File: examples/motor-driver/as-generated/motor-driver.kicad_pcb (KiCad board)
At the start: 2 copper layers, 88 x 50 mm, 12 parts, among them J1 VM 2.7-10.8V, J2 MOTOR A, J3 MOTOR B, J4 LOGIC, U1 DRV8833PW

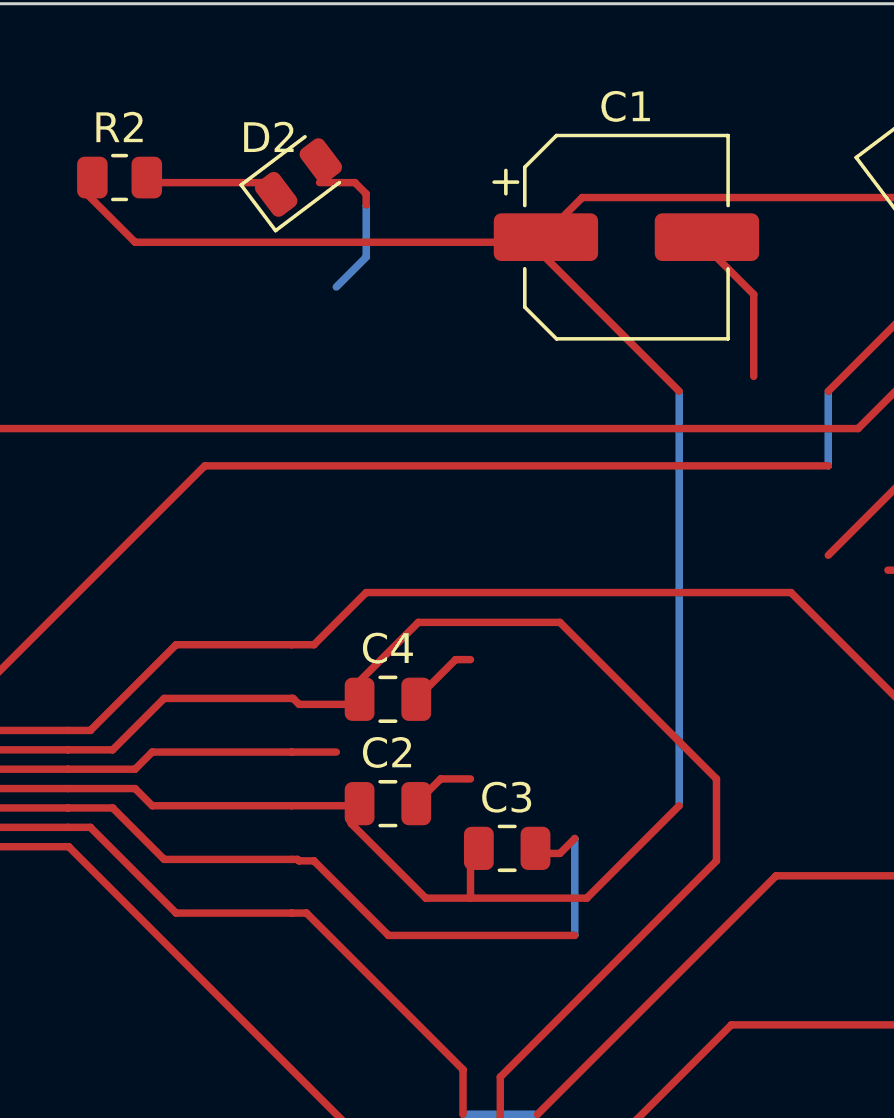
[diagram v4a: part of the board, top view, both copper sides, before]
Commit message: Give the vias room to stand beside the lands
Following the via-in-pad ban, the FPGA board stopped routing: five
attempts, five different nets, each one out of lanes in the corridor
between the FPGA's east escape fan and the codec's west one. Three
changes, in the order a layout would make them.

The via spacing was guesswork and is now the fab's. Hole to hole goes
from 1.2 mm to 0.9, which at the shipped 0.8/0.4 via leaves half a
millimetre of laminate between barrels - the ordinary minimum - and in a
1 mm-pitch escape comb is the difference between a lane and no lane.
What a via keeps off a land it may not sit in is its own radius plus a
solder-mask dam rather than the track clearance: the copper either side
may well be the same net, and what has to be true is that the mask can
part the barrel from the land.

Every decoupling capacitor now has its ground via placed against its own
pad rather than nine of them asking the search for one, and where the
via goes is chosen rather than fixed: `anchor_site` takes the nearest
position that clears everything already placed, fanning either side of
the direction facing off the part. A fixed offset walled off the
corridor its neighbour's supply needed - the via was legal, and it was
in the way.

And the seven parts sitting inside that corridor - four decoupling
capacitors, the two 1.2 V ones and the LED resistor - move four
millimetres south into the empty band below it. Twelve lanes leaving the
FPGA and ten arriving at the codec have eleven millimetres to cross in;
what a hand would do first is stop parking capacitors in the middle of
that, and it is the floorplan half of the debt this board's own README
has been carrying.

Co-Authored-By: Claude Fable 5 <noreply@anthropic.com>
Claude-Session: https://claude.ai/code/session_01DUj7Ltu92tWg159mCSacwY
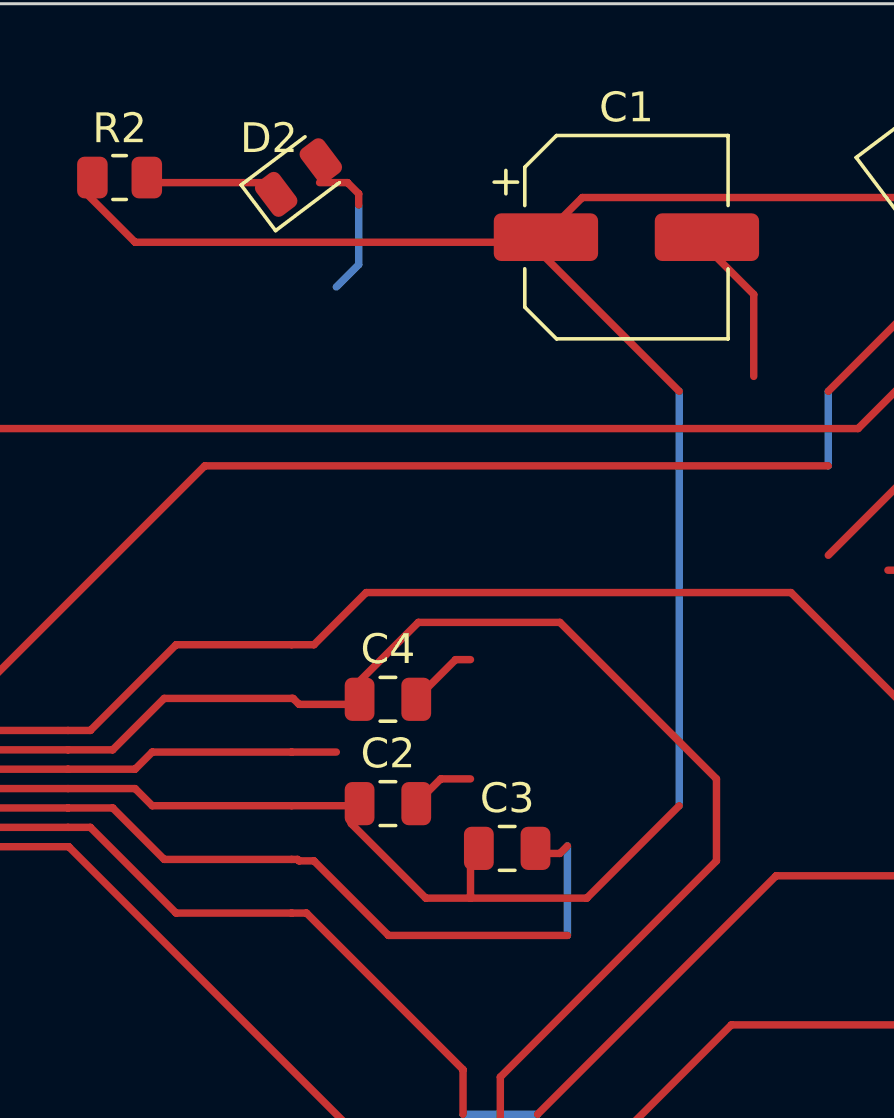
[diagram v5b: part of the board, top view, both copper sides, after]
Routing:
- net /VCP: track 27.4 -> 26.6 mm
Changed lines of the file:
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@@
 	(segment (start 181.75 97.0) (end 178.75 100.0) (width 0.25) (layer "F.Cu") (net 1))
 	(segment (start 178.75 100.0) (end 178.0 100.0) (width 0.25) (layer "F.Cu") (net 1))
-	(segment (start 158.9375 66.0) (end 160.125 66.0) (width 0.25) (layer "F.Cu") (net 1))
-	(segment (start 160.125 66.0) (end 160.5 66.375) (width 0.25) (layer "F.Cu") (net 1))
-	(segment (start 160.5 66.375) (end 160.5 66.75) (width 0.25) (layer "F.Cu") (net 1))
-	(segment (start 160.5 66.75) (end 160.5 68.5) (width 0.25) (layer "B.Cu") (net 1))
-	(segment (start 160.5 68.5) (end 159.5 69.5) (width 0.25) (layer "B.Cu") (net 1))
+	(segment (start 158.9375 66.0) (end 159.875 66.0) (width 0.25) (layer "F.Cu") (net 1))
+	(segment (start 159.875 66.0) (end 160.25 66.375) (width 0.25) (layer "F.Cu") (net 1))
+	(segment (start 160.25 66.375) (end 160.25 66.75) (width 0.25) (layer "F.Cu") (net 1))
+	(segment (start 160.25 66.75) (end 160.25 68.75) (width 0.25) (layer "B.Cu") (net 1))
+	(segment (start 160.25 68.75) (end 159.5 69.5) (width 0.25) (layer "B.Cu") (net 1))
 	(segment (start 141.1375 83.725) (end 137.5 83.725) (width 0.25) (layer "F.Cu") (net 15))
 	(segment (start 137.5 83.725) (end 134.875 81.1) (width 0.25) (layer "F.Cu") (net 15))
@@
 	(segment (start 158.25 88.75) (end 158.75 88.75) (width 0.25) (layer "F.Cu") (net 11))
 	(segment (start 158.75 88.75) (end 161.25 91.25) (width 0.25) (layer "F.Cu") (net 11))
-	(segment (start 161.25 91.25) (end 167.5 91.25) (width 0.25) (layer "F.Cu") (net 11))
+	(segment (start 161.25 91.25) (end 167.25 91.25) (width 0.25) (layer "F.Cu") (net 11))
 	(segment (start 146.8625 87.625) (end 147.0925 87.625) (width 0.25) (layer "F.Cu") (net 7))
 	(segment (start 147.0925 87.625) (end 150.5 87.625) (width 0.25) (layer "F.Cu") (net 7))
@@
 	(segment (start 151.0 66.25) (end 152.75 68.0) (width 0.25) (layer "F.Cu") (net 13))
 	(segment (start 152.75 68.0) (end 166.3 68.0) (width 0.25) (layer "F.Cu") (net 13))
-	(segment (start 167.5 91.25) (end 167.5 88.0) (width 0.25) (layer "B.Cu") (net 11))
-	(segment (start 167.5 88.0) (end 167.0 88.5) (width 0.25) (layer "F.Cu") (net 11))
+	(segment (start 167.25 91.25) (end 167.25 88.25) (width 0.25) (layer "B.Cu") (net 11))
+	(segment (start 167.25 88.25) (end 167.0 88.5) (width 0.25) (layer "F.Cu") (net 11))
 	(segment (start 167.0 88.5) (end 166.18 88.5) (width 0.25) (layer "F.Cu") (net 11))
 	(segment (start 166.18 88.5) (end 165.95 88.5) (width 0.25) (layer "F.Cu") (net 11))

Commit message: Let KiCad fill the plane, and check the fill we actually ship
The reviewer saw copper pushing in between an 0603's pads and asked
whether DRC had been run at all. It had, and it was green, and both
things were true because the check and the drawing were looking at
different polygons.

The fill in the file was ours: a sweep of the pour outline with
everything of another net subtracted, written because a note here said
KiCad's own filler needs a display the container has not got. It does
not - `pcbnew`'s `ZONE_FILLER` runs headless in both images, and always
did by the time that note was written. Meanwhile `pcb drc` was passing
`--refill-zones`, so KiCad threw our polygons away and reported on a
fill of its own. Nobody was checking the one that ships, and it had
drifted: copper 0.075 mm from a foreign pad where the rule says 0.25,
and - measured just now with the refill turned off - two hundred pieces
of copper KiCad calls isolated.

So the zone is declared and left empty, and KiCad fills it: clearance,
minimum width and thermal relief all come from the board's own rules
instead of this file's idea of them. And `drc()` no longer refills a
board whose zones are already filled, because that fill is what goes to
the fab and what the plots draw. A board with an unfilled zone is still
refilled - otherwise every pad on that net reads as unconnected and the
report is noise - and `layout.unfilled_zone` says the file is
incomplete.

All five boards regenerate clean on both matrix versions against their
own committed fill: no errors, nothing unconnected, no isolated copper.
The plane no longer reaches between the passives' lands, and every
through-hole ground pad now has the four spokes of a thermal relief, so
an iron can bring the joint up without heating the whole plane.

The parser gains a pad's corner radius while measuring this, because a
roundrect land's bounding box is a quarter of a millimetre away from
where its copper is.

Co-Authored-By: Claude Fable 5 <noreply@anthr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
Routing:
- net GND: track 68.0 -> 66.2 mm
- net /LED_A: track 4.15 -> 5.99 mm

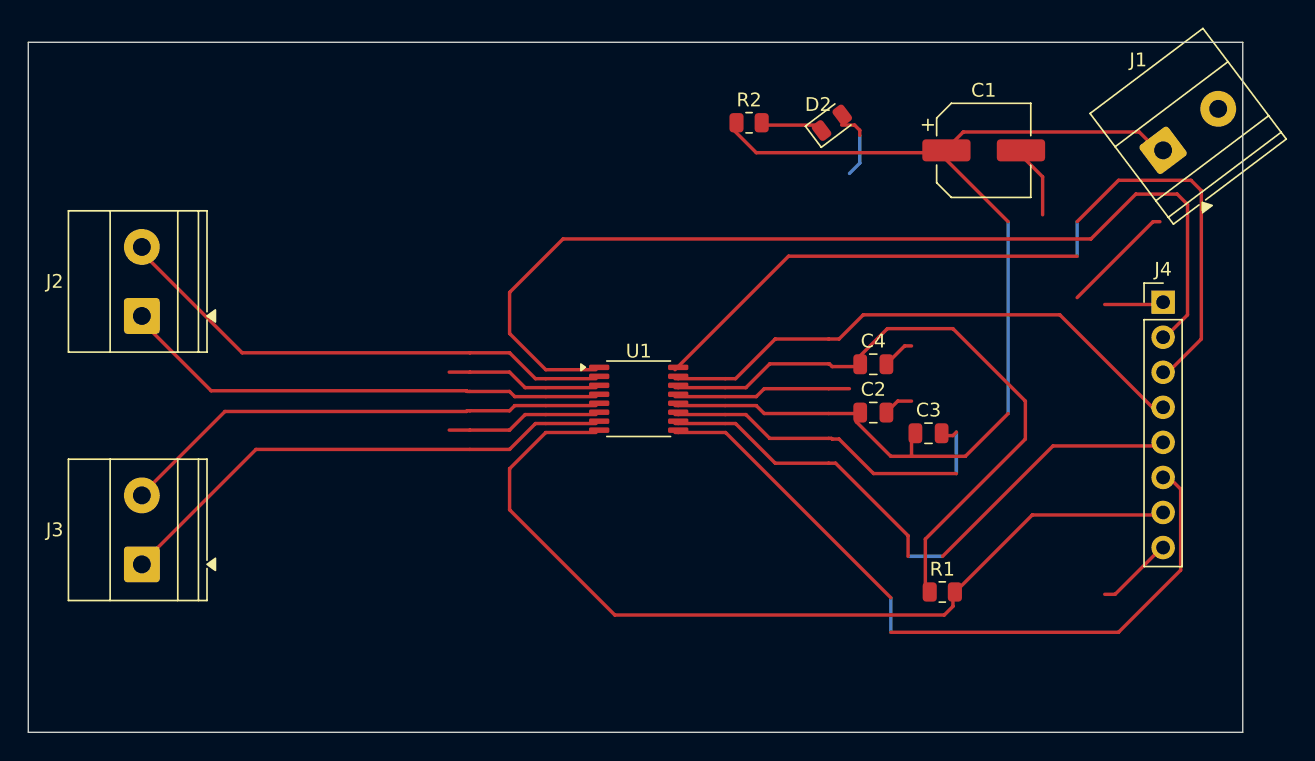
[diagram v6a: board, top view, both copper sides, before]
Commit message: Relieve the pads, fillet the joints, and give the board its screw holes
Three of the reviewer's manufacturing points, and they largely fall out
of the one before it - once KiCad fills the plane, the thermal relief it
was already asked for in the file actually appears.

**Thermal relief.** The zones said thermal all along; our own filler
ignored it and flooded every land solid. KiCad's does not, so every
through-hole ground pad now sits in a gap bridged by four spokes and an
iron can bring the joint up without heating a hundred square millimetres
of copper. `layout.solid_pad_connection` reports the setting when a
board turns it off: drilled pads only, because a surface pad reflows in
an oven that is heating the plane anyway and flooding it is often the
better thermal answer.

**Teardrops.** A track entering a land is a step change in width, and a
step change is where copper tears - the connector gets levered on and
off, the drill wanders, and the crack starts at the corner. `_teardrops`
replaces the first stretch of each run with a three-step taper into the
land, checked against its neighbours before it is kept, so a fillet
never eats the clearance a fine-pitch escape needs. It *replaces* rather
than overlays: laying the taper on top of the run drew the same copper
twice, and `route.acute_angle` reported all thirty of them, correctly.
`route.mixed_track_widths` learns what a fillet looks like so a properly
filleted board does not read as one nobody decided the width of.

**Mounting holes.** Four M3 holes near the corners, placed before the
router runs because they are obstacles, and slid along the edges or a
little inboard where a connector body has the corner - the motor board
and the op-amp take three, which is what those floorplans have room for.
Grounded on the motor driver, whose chassis is metal and part of the
shield, plain on the rest: bonding the enclosure to the reference is the
enclosure's decision, not the board's.

Two things that fell out of placing par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
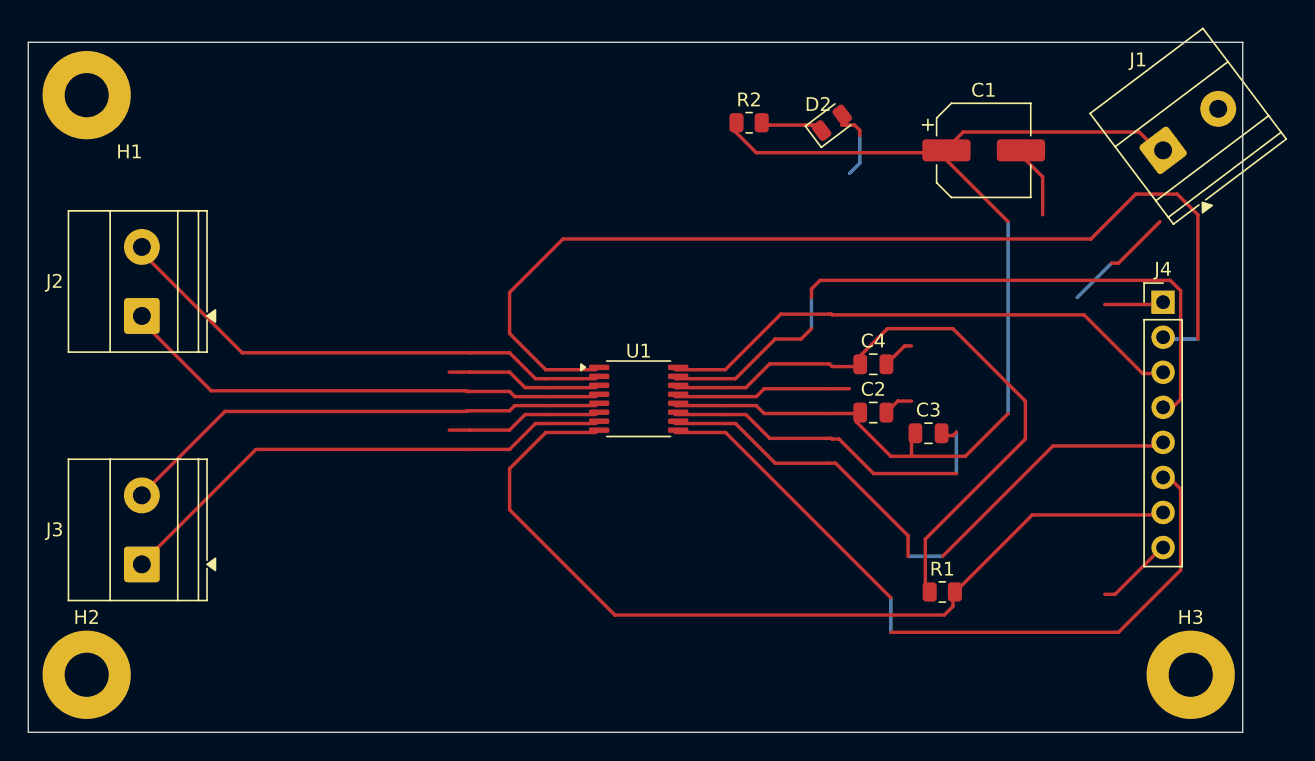
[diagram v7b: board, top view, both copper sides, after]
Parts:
- added H1: M33, MountingHole:MountingHole_3.2mm_M3_Pad, F.Cu at (104.2, 63.8)
- added H2: M33, MountingHole:MountingHole_3.2mm_M3_Pad, F.Cu at (104.2, 105.8)
- added H3: M33, MountingHole:MountingHole_3.2mm_M3_Pad, F.Cu at (184.2, 105.8)
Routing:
- net /AIN1: track 60.4 -> 38.6 mm
- net /AIN2: track 39.9 -> 51.3 mm
- net /nSLEEP: track 73.5 -> 75.5 mm

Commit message: Give the assembly machine something to aim at
Fiducials: three copper dots in bare mask windows, near three different
corners so a pick-and-place gets rotation as well as offset. It aligns
to the board, not to the drawing - without them it has only the routed
outline, cut to a tolerance ten times looser than the placement a 0.5 mm
pitch part is asking for. `fab.no_fiducials` reports a fine-pitch board
that has none, as context rather than as a fault: plenty of boards are
built one at a time with tweezers.

They share the corner search with the mounting holes, which is where
this found a real bug: `_courtyard_box` read lines and rectangles only,
and a mounting hole draws its courtyard as one circle - so every hole
measured as taking up no room at all, and the first three fiducials
landed on top of three screw holes. Circles and arcs count now.

Co-Authored-By: Claude Fable 5 <noreply@anthropic.com>
Claude-Session: https://claude.ai/code/session_01DUj7Ltu92tWg159mCSacwY
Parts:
- added FID1: Fiducial, Fiducial:Fiducial_1mm_Mask2mm, F.Cu at (109.7, 62.3)
- added FID2: Fiducial, Fiducial:Fiducial_1mm_Mask2mm, F.Cu at (185.7, 62.3)
- added FID3: Fiducial, Fiducial:Fiducial_1mm_Mask2mm, F.Cu at (109.7, 107.3)
- H1, H2, H3: value M33 -> M3
